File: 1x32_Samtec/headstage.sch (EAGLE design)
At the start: 15 parts, among them U1 RHD2132_QFN

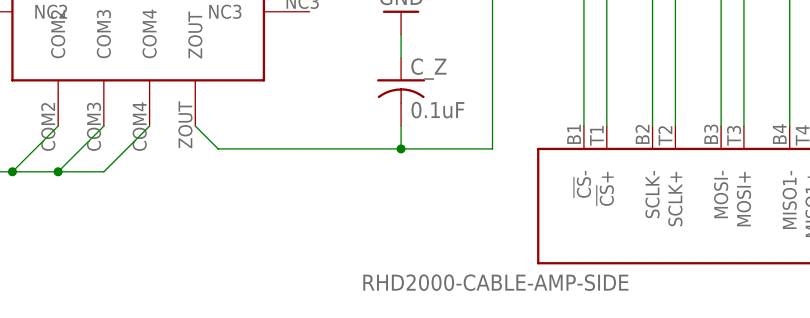
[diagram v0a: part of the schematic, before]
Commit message: Replaced samtec design with updated samtec design (2.1)
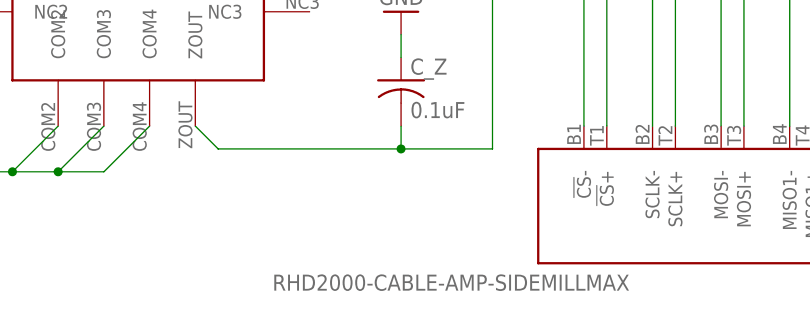
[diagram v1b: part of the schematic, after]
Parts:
- S2: value RHD2000-CABLE-AMP-SIDE -> RHD2000-CABLE-AMP-SIDEMILLMAX; device RHD2000:RHD2000-CABLE-AMP-SIDE -> RHD2000:RHD2000-CABLE-AMP-SIDEMILLMAX
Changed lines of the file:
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@@
 <?xml version="1.0" encoding="utf-8"?>
 <!DOCTYPE eagle SYSTEM "eagle.dtd">
-<eagle version="6.4">
+<eagle version="6.5.0">
 <drawing>
 <settings>
@@
 <parts>
 <part name="U$1" library="voigts" deviceset="ADXL335" device=""/>
-<part name="S2" library="RHD2000" deviceset="RHD2000-CABLE-AMP-SIDE" device=""/>
+<part name="S2" library="RHD2000" deviceset="RHD2000-CABLE-AMP-SIDE" device="MILLMAX" value="RHD2000-CABLE-AMP-SIDEMILLMAX"/>
 <part name="U1" library="RHD2000" deviceset="RHD2132" device="_QFN"/>
 <part name="R1" library="resistor" deviceset="R-EU_" device="R0402" value="100"/>
